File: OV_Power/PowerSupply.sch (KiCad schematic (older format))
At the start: 15 parts, among them J1 OpenVent_Barrel_Connector, U5 CSD88537ND, U6 LTC4365xTS8, U7 LTC4416, U8 AOSD21307, U9 AOSD21307

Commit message: Sorted out the interconnect between power supply and main boards.
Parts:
- added J?: Conn_HDR_2x10_latching, F_Misc:3M_D3428-6302-AR, symbol OpenVent:Conn_HDR_2x10_latching
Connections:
- net labels added: CHG_CURRENT, MOTOR-IN-A, MOTOR-IN-B, PWM, V7.5V, V7.5V_EN, nMOTOR-FAULT-A, nMOTOR-FAULT-B
- wire segments 103 -> 131
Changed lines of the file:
@@
 Text Notes 700  2750 0    50   ~ 0
 INPUT SHOULD BE FUSED.\nA FERRITE MIGHT BE REQUIRED\nFOR EMI SUPPRESSION.\nA TVS SHOULD ALSO BE\nADDED FOR ESD PROTECTION.
+$Comp
+L OpenVent:Conn_HDR_2x10_latching J?
+U 1 1 5FB4D557
+P 2500 5000
+F 0 "J?" H 2550 5617 50  0000 C CNN
+F 1 "Conn_HDR_2x10_latching" H 2550 5526 50  0001 C CNN
+F 2 "F_Misc:3M_D3428-6302-AR" H 2500 5000 50  0001 C CNN
+F 3 "https://multimedia.3m.com/mws/media/485761O/3mtm-four-wall-header-ts2245.pdf" H 2500 5000 50  0001 C CNN
+F 4 "CONN HEADER VERT 20POS 2.54MM LATCHING" H 2500 5000 50  0001 C CNN "Desc"
+F 5 "Connector Header Through Hole 20 position 0.100\" (2.54mm) with latches" H 2500 5000 50  0001 C CNN "Detailed"
+F 6 "3M" H 2500 5000 50  0001 C CNN "Mfr"
+F 7 "D3428-6302-AR" H 2550 5526 50  0000 C CNN "Mfr_PN"
+	1    2500 5000
+	1    0    0    -1
+$EndComp
+$Comp
+L OpenVent:GND #PWR?
+U 1 1 5FB4E8B3
+P 2900 5550
+F 0 "#PWR?" H 2900 5300 50  0001 C CNN
+F 1 "GND" H 2900 5400 50  0001 C CNN
+F 2 "" H 2900 5550 50  0001 C CNN
+F 3 "" H 2900 5550 50  0001 C CNN
+	1    2900 5550
+	1    0    0    -1
+$EndComp
+$Comp
+L OpenVent:GND #PWR?
+U 1 1 5FB4EC42
+P 2000 4500
+F 0 "#PWR?" H 2000 4250 50  0001 C CNN
+F 1 "GND" H 2000 4350 50  0001 C CNN
+F 2 "" H 2000 4500 50  0001 C CNN
+F 3 "" H 2000 4500 50  0001 C CNN
+	1    2000 4500
+	1    0    0    -1
+$EndComp
+$Comp
+L OpenVent:V_MAIN #PWR?
+U 1 1 5FB4F4C3
+P 1850 4500
+F 0 "#PWR?" H 1850 4350 50  0001 C CNN
+F 1 "V_MAIN" H 1850 4673 50  0000 C CNN
+F 2 "" H 1850 4500 50  0001 C CNN
+F 3 "" H 1850 4500 50  0001 C CNN
+	1    1850 4500
+	1    0    0    -1
+$EndComp
+$Comp
+L OpenVent:V_MAIN #PWR?
+U 1 1 5FB4FD2E
+P 3100 4500
+F 0 "#PWR?" H 3100 4350 50  0001 C CNN
+F 1 "V_MAIN" H 3100 4673 50  0000 C CNN
+F 2 "" H 3100 4500 50  0001 C CNN
+F 3 "" H 3100 4500 50  0001 C CNN
+	1    3100 4500
+	1    0    0    -1
+$EndComp
+Text GLabel 1800 5500 0    50   Input ~ 0
+V7.5V
+Text GLabel 3150 5400 2    50   Input ~ 0
+V7.5V
+Text GLabel 3150 5300 2    50   Output ~ 0
+V7.5V_EN
+Wire Wire Line
+	2900 5550 2900 5500
+Wire Wire Line
+	2900 5500 2800 5500
+Wire Wire Line
+	2300 4600 2100 4600
+Wire Wire Line
+	2100 4600 2100 4500
+Wire Wire Line
+	2100 4500 2000 4500
+Wire Wire Line
+	2800 4600 3100 4600
+Wire Wire Line
+	3100 4600 3100 4500
+Wire Wire Line
+	2300 4700 1850 4700
+Wire Wire Line
+	1850 4700 1850 4500
+Wire Wire Line
+	2300 5500 1800 5500
+Wire Wire Line
+	3150 5400 2800 5400
+Wire Wire Line
+	3150 5300 2800 5300
+$Comp
+L OpenVent:VBATT #PWR?
+U 1 1 5FB6E37F
+P 3400 4500
+F 0 "#PWR?" H 3400 4350 50  0001 C CNN
+F 1 "VBATT" H 3400 4673 50  0000 C CNN
+F 2 "" H 3400 4500 50  0001 C CNN
+F 3 "" H 3400 4500 50  0001 C CNN
+	1    3400 4500
+	1    0    0    -1
+$EndComp
+Wire Wire Line
+	2800 4700 3400 4700
+Wire Wire Line
+	3400 4700 3400 4500
+Text GLabel 1800 5000 0    60   Output ~ 0
+PWM
+Text GLabel 1800 4900 0    60   Output ~ 0
+MOTOR-IN-A
+Text GLabel 3150 4900 2    60   Output ~ 0
+MOTOR-IN-B
+Text GLabel 1800 4800 0    60   Input ~ 0
+nMOTOR-FAULT-A
+Text GLabel 3150 4800 2    60   Input ~ 0
+nMOTOR-FAULT-B
+Wire Wire Line
+	4200 2600 4400 2600
+Wire Wire Line
+	1800 4800 2300 4800
+Wire Wire Line
+	2800 4800 3150 4800
+Wire Wire Line
+	1800 4900 2300 4900
+Wire Wire Line
+	3150 4900 2800 4900
+Wire Wire Line
+	2300 5000 1800 5000
+Text GLabel 1800 5400 0    50   Input ~ 0
+CHG_CURRENT
+Wire Wire Line
+	2300 5400 1800 5400
+Wire Wire Line
+	2800 5100 4400 5100
+Wire Wire Line
+	4400 2600 4400 5100
+$Comp
+L OpenVent:GND #PWR?
+U 1 1 5FBAF99A
+P 4300 4950
+F 0 "#PWR?" H 4300 4700 50  0001 C CNN
+F 1 "GND" H 4300 4800 50  0001 C CNN
+F 2 "" H 4300 4950 50  0001 C CNN
+F 3 "" H 4300 4950 50  0001 C CNN
+	1    4300 4950
+	1    0    0    -1
+$EndComp
+Wire Wire Line
+	2800 5000 4150 5000
+Wire Wire Line
+	4150 5000 4150 4950
+Wire Wire Line
+	4150 4950 4300 4950
+$Comp
+L OpenVent:VIN_12V #PWR?
+U 1 1 5FBA1DE1
+P 700 5050
+F 0 "#PWR?" H 700 4900 50  0001 C CNN
+F 1 "VIN_12V" H 700 5223 50  0000 C CNN
+F 2 "" H 700 5050 60  0001 C CNN
+F 3 "" H 700 5050 60  0001 C CNN
+	1    700  5050
+	1    0    0    -1
+$EndComp
+Wire Wire Line
+	2300 5100 700  5100
+Wire Wire Line
+	700  5100 700  5050
 $EndSCHEMATC

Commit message: First cut at a placement study for the power board.
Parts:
- R32, R33, R34, R35, R36, R37, R38, R39: footprint (none) -> Resistor_SMD:R_0603_1608Metric
- gave numbers to parts that had none: 1
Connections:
- net labels added: MOTOR-CURRENT
- wire segments 131 -> 130
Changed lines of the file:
@@
 F 0 "R35" V 3104 2070 50  0000 L CNN
 F 1 "R_0603_510K_0.1W_1%" H 3050 2100 50  0001 C CNN
-F 2 "" H 3050 2100 60  0001 C CNN
+F 2 "Resistor_SMD:R_0603_1608Metric" H 3050 2100 60  0001 C CNN
 F 3 "" H 3050 2100 60  0001 C CNN
 F 4 "510K" V 3195 2070 50  0000 L CNN "Val"
@@
 F 0 "R32" V 2704 2070 50  0000 L CNN
 F 1 "R_0603_4.53M_0.1W_5%" H 2650 2100 50  0001 C CNN
-F 2 "" H 2650 2100 60  0001 C CNN
+F 2 "Resistor_SMD:R_0603_1608Metric" H 2650 2100 60  0001 C CNN
 F 3 "" H 2650 2100 60  0001 C CNN
 F 4 "4.53M" V 2795 2070 50  0000 L CNN "Val"
@@
 F 0 "R33" V 2704 2570 50  0000 L CNN
 F 1 "R_0603_169K_0.1W_1%" H 2650 2600 50  0001 C CNN
-F 2 "" H 2650 2600 60  0001 C CNN
+F 2 "Resistor_SMD:R_0603_1608Metric" H 2650 2600 60  0001 C CNN
 F 3 "" H 2650 2600 60  0001 C CNN
 F 4 "169K" V 2795 2570 50  0000 L CNN "Val"
@@
 F 0 "R34" V 2704 3070 50  0000 L CNN
 F 1 "R_0603_133K_0.1W_1%" H 2650 3100 50  0001 C CNN
-F 2 "" H 2650 3100 60  0001 C CNN
+F 2 "Resistor_SMD:R_0603_1608Metric" H 2650 3100 60  0001 C CNN
 F 3 "" H 2650 3100 60  0001 C CNN
 F 4 "133K" V 2795 3070 50  0000 L CNN "Val"
@@
 F 0 "R39" V 6354 1970 50  0000 L CNN
 F 1 "10k_0603_Chip_Resistor,_1%,_0.1W" H 6300 2000 50  0001 C CNN
-F 2 "" H 6300 2000 50  0001 C CNN
+F 2 "Resistor_SMD:R_0603_1608Metric" H 6300 2000 50  0001 C CNN
 F 3 "" H 6300 2000 50  0001 C CNN
 F 4 "10k" V 6445 1970 50  0000 L CNN "Val"
@@
 F 0 "R37" V 5854 2470 50  0000 L CNN
 F 1 "R_0603_24k9_0.1W_1%" H 5800 2500 50  0001 C CNN
-F 2 "" H 5800 2500 60  0001 C CNN
+F 2 "Resistor_SMD:R_0603_1608Metric" H 5800 2500 60  0001 C CNN
 F 3 "" H 5800 2500 60  0001 C CNN
 F 4 "24k9" V 5945 2470 50  0000 L CNN "Val"
@@
 F 0 "R38" H 5900 3043 50  0000 C CNN
 F 1 "R_0603_221K_0.1W_1%" H 5800 3350 50  0001 C CNN
-F 2 "" H 5800 3350 60  0001 C CNN
+F 2 "Resistor_SMD:R_0603_1608Metric" H 5800 3350 60  0001 C CNN
 F 3 "" H 5800 3350 60  0001 C CNN
 F 4 "221K" H 5900 3134 50  0000 C CNN "Val"
@@
 F 0 "R36" V 5854 1970 50  0000 L CNN
 F 1 "R_0603_178K_0.1W_1%" H 5800 2000 50  0001 C CNN
-F 2 "" H 5800 2000 60  0001 C CNN
+F 2 "Resistor_SMD:R_0603_1608Metric" H 5800 2000 60  0001 C CNN
 F 3 "" H 5800 2000 60  0001 C CNN
 F 4 "178K" V 5945 1970 50  0000 L CNN "Val"
@@
 INPUT SHOULD BE FUSED.\nA FERRITE MIGHT BE REQUIRED\nFOR EMI SUPPRESSION.\nA TVS SHOULD ALSO BE\nADDED FOR ESD PROTECTION.
 $Comp
-L OpenVent:Conn_HDR_2x10_latching J?
+L OpenVent:Conn_HDR_2x10_latching J2
 U 1 1 5FB4D557
 P 2500 5000
-F 0 "J?" H 2550 5617 50  0000 C CNN
+F 0 "J2" H 2550 5617 50  0000 C CNN
 F 1 "Conn_HDR_2x10_latching" H 2550 5526 50  0001 C CNN
 F 2 "F_Misc:3M_D3428-6302-AR" H 2500 5000 50  0001 C CNN
@@
 $EndComp
 $Comp
-L OpenVent:GND #PWR?
+L OpenVent:GND #PWR030
 U 1 1 5FB4E8B3
 P 2900 5550
-F 0 "#PWR?" H 2900 5300 50  0001 C CNN
+F 0 "#PWR030" H 2900 5300 50  0001 C CNN
 F 1 "GND" H 2900 5400 50  0001 C CNN
 F 2 "" H 2900 5550 50  0001 C CNN
@@
 $EndComp
 $Comp
-L OpenVent:GND #PWR?
+L OpenVent:GND #PWR018
 U 1 1 5FB4EC42
 P 2000 4500
-F 0 "#PWR?" H 2000 4250 50  0001 C CNN
+F 0 "#PWR018" H 2000 4250 50  0001 C CNN
 F 1 "GND" H 2000 4350 50  0001 C CNN
 F 2 "" H 2000 4500 50  0001 C CNN
@@
 $EndComp
 $Comp
-L OpenVent:V_MAIN #PWR?
-U 1 1 5FB4F4C3
-P 1850 4500
-F 0 "#PWR?" H 1850 4350 50  0001 C CNN
-F 1 "V_MAIN" H 1850 4673 50  0000 C CNN
-F 2 "" H 1850 4500 50  0001 C CNN
-F 3 "" H 1850 4500 50  0001 C CNN
-	1    1850 4500
-	1    0    0    -1
-$EndComp
-$Comp
-L OpenVent:V_MAIN #PWR?
+L OpenVent:V_MAIN #PWR031
 U 1 1 5FB4FD2E
 P 3100 4500
-F 0 "#PWR?" H 3100 4350 50  0001 C CNN
+F 0 "#PWR031" H 3100 4350 50  0001 C CNN
 F 1 "V_MAIN" H 3100 4673 50  0000 C CNN
 F 2 "" H 3100 4500 50  0001 C CNN
@@
 	3100 4600 3100 4500
 Wire Wire Line
-	2300 4700 1850 4700
-Wire Wire Line
-	1850 4700 1850 4500
-Wire Wire Line
 	2300 5500 1800 5500
 Wire Wire Line
@@
 	3150 5300 2800 5300
 $Comp
-L OpenVent:VBATT #PWR?
+L OpenVent:VBATT #PWR032
 U 1 1 5FB6E37F
 P 3400 4500
-F 0 "#PWR?" H 3400 4350 50  0001 C CNN
+F 0 "#PWR032" H 3400 4350 50  0001 C CNN
 F 1 "VBATT" H 3400 4673 50  0000 C CNN
 F 2 "" H 3400 4500 50  0001 C CNN
@@
 	4400 2600 4400 5100
 $Comp
-L OpenVent:GND #PWR?
+L OpenVent:GND #PWR033
 U 1 1 5FBAF99A
 P 4300 4950
-F 0 "#PWR?" H 4300 4700 50  0001 C CNN
+F 0 "#PWR033" H 4300 4700 50  0001 C CNN
 F 1 "GND" H 4300 4800 50  0001 C CNN
 F 2 "" H 4300 4950 50  0001 C CNN
@@
 	4150 4950 4300 4950
 $Comp
-L OpenVent:VIN_12V #PWR?
+L OpenVent:VIN_12V #PWR017
 U 1 1 5FBA1DE1
 P 700 5050
-F 0 "#PWR?" H 700 4900 50  0001 C CNN
+F 0 "#PWR017" H 700 4900 50  0001 C CNN
 F 1 "VIN_12V" H 700 5223 50  0000 C CNN
 F 2 "" H 700 5050 60  0001 C CNN
@@
 Wire Wire Line
 	700  5100 700  5050
+Text GLabel 1800 5200 0    50   Input ~ 0
+MOTOR-CURRENT
+Wire Wire Line
+	2300 5200 1800 5200
 $EndSCHEMATC

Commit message: New board outline and power connector added.  Still need definition of connector for microswitches and schematic.
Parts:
- removed J1: OpenVent_Barrel_Connector, Connector_BarrelJack:BarrelJack_CUI_PJ-102AH_Horizontal, symbol OpenVent:OpenVent_Barrel_Connector
- added J1: Kycon_kpjx-4s, OpenVent:Kycon_KPJX-4S, symbol OpenVent:Kycon_kpjx-4s
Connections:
- wire segments 130 -> 140
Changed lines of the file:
@@
 L OpenVent:GND #GND_?
 U 1 1 5FBB7C1D
-P 1400 2200
+P 1050 2050
 AR Path="/5FBB7C1D" Ref="#GND_?"  Part="1"
 AR Path="/5FAE643E/5FBB7C1D" Ref="#GND_017"  Part="1"
-F 0 "#GND_017" H 1400 2200 20  0001 C CNN
-F 1 "GND" H 1400 2130 30  0001 C CNN
-F 2 "" H 1400 2200 70  0001 C CNN
-F 3 "" H 1400 2200 70  0001 C CNN
-	1    1400 2200
-	1    0    0    -1
-$EndComp
-Wire Wire Line
-	1400 1900 1150 1900
-$Comp
-L OpenVent:OpenVent_Barrel_Connector J?
-U 1 1 5FBB7C29
-P 1050 1900
-AR Path="/5FBB7C29" Ref="J?"  Part="1"
-AR Path="/5FAE643E/5FBB7C29" Ref="J1"  Part="1"
-F 0 "J1" H 957 2325 50  0000 C CNN
-F 1 "OpenVent_Barrel_Connector" H 740 1770 50  0001 L BNN
-F 2 "Connector_BarrelJack:BarrelJack_CUI_PJ-102AH_Horizontal" H 1050 1900 50  0001 C CNN
-F 3 "https://www.cuidevices.com/product/resource/digikeypdf/pj-102ah.pdf" H 1050 1900 50  0001 C CNN
-F 4 "PJ-102AH" H 957 2234 50  0000 C CNN "Mfr_PN"
-F 5 "CUI Devices" H 1050 1900 50  0001 C CNN "Mfr"
-F 6 "DigiKey" H 1050 1900 50  0001 C CNN "DistName"
-F 7 "CP-102AH-ND" H 1050 1900 50  0001 C CNN "Dist_PN"
-F 8 "Power Barrel Connector Jack 2.00mm ID (0.079\"), 5.50mm OD (0.217\") Through Hole, Right Angle" H 1050 1900 50  0001 C CNN "Detailed"
-	1    1050 1900
-	1    0    0    -1
-$EndComp
-Wire Wire Line
-	1400 1900 1400 2200
-Wire Wire Line
-	1150 1700 2550 1700
-Connection ~ 2550 1700
-Text Notes 1200 1250 0    50   ~ 0
+F 0 "#GND_017" H 1050 2050 20  0001 C CNN
+F 1 "GND" H 1050 1980 30  0001 C CNN
+F 2 "" H 1050 2050 70  0001 C CNN
+F 3 "" H 1050 2050 70  0001 C CNN
+	1    1050 2050
+	1    0    0    -1
+$EndComp
+Text Notes 1050 950  0    50   ~ 0
 LTC4365 provides reverse polarity protection\nUndervoltage lockout: 8V\nOvervoltage lockout: 18V
 Wire Notes Line
-	1150 950  3000 950
+	1000 650  2850 650
 Wire Notes Line
-	3000 950  3000 1300
+	2850 650  2850 1000
 Wire Notes Line
-	3000 1300 1150 1300
+	2850 1000 1000 1000
 Wire Notes Line
-	1150 1300 1150 950
+	1000 1000 1000 650
 $Comp
 L OpenVent:LTC4416 U7
@@
 	6750 3700 6750 3650
 Connection ~ 7150 3400
-Text Notes 700  2750 0    50   ~ 0
+Text Notes 600  2650 0    50   ~ 0
 INPUT SHOULD BE FUSED.\nA FERRITE MIGHT BE REQUIRED\nFOR EMI SUPPRESSION.\nA TVS SHOULD ALSO BE\nADDED FOR ESD PROTECTION.
 $Comp
@@
 Wire Wire Line
 	2300 5200 1800 5200
+$Comp
+L OpenVent:Kycon_kpjx-4s J1
+U 1 1 5FBCEB95
+P 1050 1700
+F 0 "J1" H 1050 2067 50  0000 C CNN
+F 1 "Kycon_kpjx-4s" H 1050 1976 50  0000 C CNN
+F 2 "OpenVent:Kycon_KPJX-4S" H 1050 1700 50  0001 C CNN
+F 3 "http://www.kycon.com/Pub_Eng_Draw/KPJX-4S.pdf" H 1050 1700 50  0001 C CNN
+F 4 "Kycon, Inc." H 1050 1700 50  0001 C CNN "Mfr"
+F 5 "KPJX-4S" H 1050 1700 50  0001 C CNN "Mfr_PN"
+F 6 "4 (Power) Position Circular Connector Jack, Female Sockets Solder" H 1050 1700 50  0001 C CNN "Detailed"
+F 7 "CONN JACK FMALE 4POS TIN SOLDER" H 1050 1700 50  0001 C CNN "Desc"
+	1    1050 1700
+	1    0    0    -1
+$EndComp
+Wire Wire Line
+	2550 1700 1500 1700
+Connection ~ 2550 1700
+Wire Wire Line
+	750  1600 650  1600
+Wire Wire Line
+	650  1600 650  1250
+Wire Wire Line
+	650  1250 1500 1250
+Wire Wire Line
+	1500 1250 1500 1700
+Connection ~ 1500 1700
+Wire Wire Line
+	1500 1700 1350 1700
+Wire Wire Line
+	1350 1600 1400 1600
+Wire Wire Line
+	1400 1600 1400 2000
+Wire Wire Line
+	1400 2000 1050 2000
+Wire Wire Line
+	700  2000 700  1700
+Wire Wire Line
+	700  1700 750  1700
+Wire Wire Line
+	1050 2000 1050 2050
+Connection ~ 1050 2000
+Wire Wire Line
+	1050 2000 700  2000
 $EndSCHEMATC

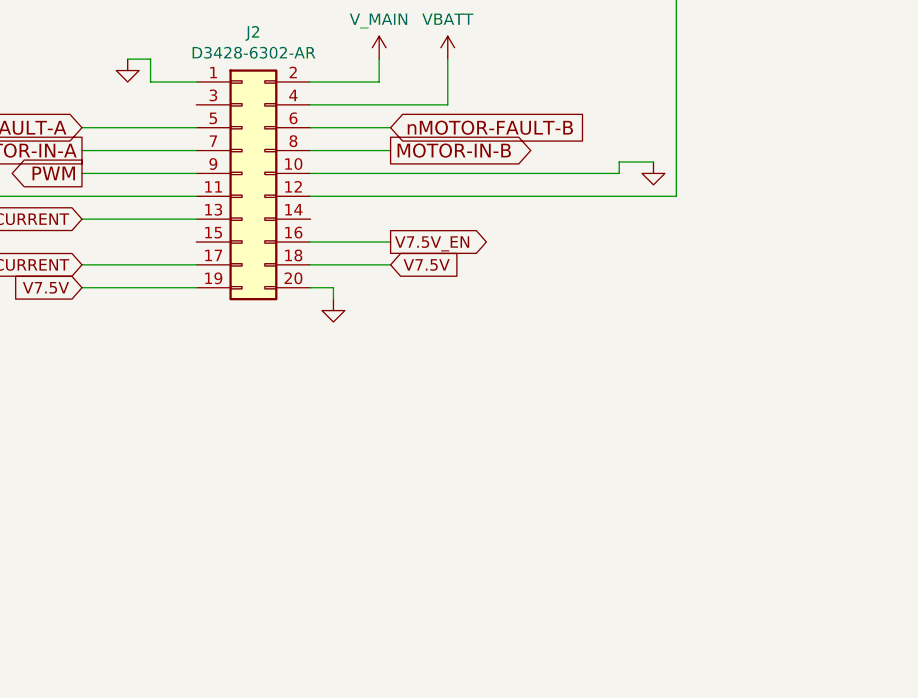
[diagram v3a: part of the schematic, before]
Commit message: Continuing to refine both the schemo and placement for the power supply board.  I think we have all the connectors we need now...
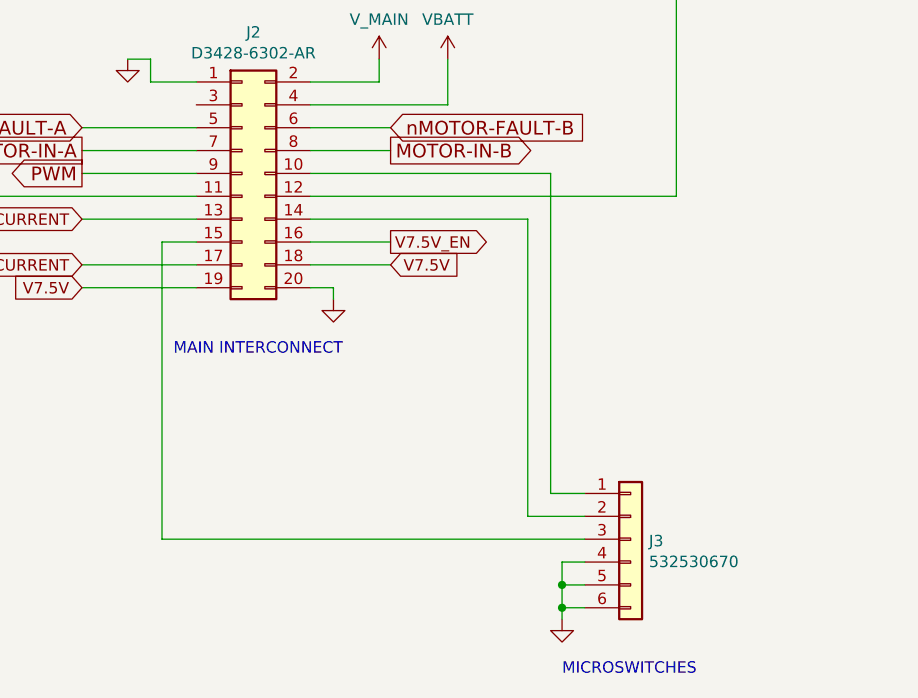
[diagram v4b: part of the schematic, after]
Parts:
- added J3: 532530670, Connector_Molex:Molex_Micro-Latch_53253-0670_1x06_P2.00mm_Vertical, symbol OpenVent:532530670
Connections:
- wire segments 140 -> 152
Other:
- note added: "MAIN INTERCONNECT"
- note added: "MICROSWITCHES"
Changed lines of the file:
@@
 	4400 2600 4400 5100
-$Comp
-L OpenVent:GND #PWR033
-U 1 1 5FBAF99A
-P 4300 4950
-F 0 "#PWR033" H 4300 4700 50  0001 C CNN
-F 1 "GND" H 4300 4800 50  0001 C CNN
-F 2 "" H 4300 4950 50  0001 C CNN
-F 3 "" H 4300 4950 50  0001 C CNN
-	1    4300 4950
-	1    0    0    -1
-$EndComp
-Wire Wire Line
-	2800 5000 4150 5000
-Wire Wire Line
-	4150 5000 4150 4950
-Wire Wire Line
-	4150 4950 4300 4950
 $Comp
 L OpenVent:VIN_12V #PWR017
@@
 Wire Wire Line
 	1050 2000 700  2000
+$Comp
+L OpenVent:532530670 J3
+U 1 1 5FC7E477
+P 4200 6600
+F 0 "J3" H 4280 6592 50  0000 L CNN
+F 1 "532530670" H 4280 6501 50  0000 L CNN
+F 2 "Connector_Molex:Molex_Micro-Latch_53253-0670_1x06_P2.00mm_Vertical" H 4200 6600 50  0001 C CNN
+F 3 "https://www.molex.com/pdm_docs/sd/532530270_sd.pdf" H 4200 6600 50  0001 C CNN
+F 4 "Molex" H 4200 6600 50  0001 C CNN "Mfr"
+F 5 "0532530670" H 4200 6600 50  0001 C CNN "Mfr_PN"
+F 6 "CONN HEADER VERT 6POS 2MM" H 4200 6600 50  0001 C CNN "Desc"
+F 7 "Connector Header Through Hole 6 position 0.079\" (2.00mm)" H 4200 6600 50  0001 C CNN "Detailed"
+	1    4200 6600
+	1    0    0    -1
+$EndComp
+$Comp
+L OpenVent:GND #PWR033
+U 1 1 5FC7F729
+P 3900 6950
+F 0 "#PWR033" H 3900 6700 50  0001 C CNN
+F 1 "GND" H 3900 6800 50  0001 C CNN
+F 2 "" H 3900 6950 50  0001 C CNN
+F 3 "" H 3900 6950 50  0001 C CNN
+	1    3900 6950
+	1    0    0    -1
+$EndComp
+Wire Wire Line
+	4000 6700 3900 6700
+Wire Wire Line
+	3900 6700 3900 6800
+Wire Wire Line
+	4000 6800 3900 6800
+Connection ~ 3900 6800
+Wire Wire Line
+	3900 6800 3900 6900
+Wire Wire Line
+	4000 6900 3900 6900
+Connection ~ 3900 6900
+Wire Wire Line
+	3900 6900 3900 6950
+Wire Wire Line
+	4000 6600 2150 6600
+Wire Wire Line
+	2150 6600 2150 5300
+Wire Wire Line
+	2150 5300 2300 5300
+Wire Wire Line
+	4000 6500 3750 6500
+Wire Wire Line
+	3750 6500 3750 5200
+Wire Wire Line
+	3750 5200 2800 5200
+Wire Wire Line
+	2800 5000 3850 5000
+Wire Wire Line
+	3850 5000 3850 6400
+Wire Wire Line
+	3850 6400 4000 6400
+Text Notes 2200 5800 0    50   ~ 0
+MAIN INTERCONNECT
+Text Notes 3900 7200 0    50   ~ 0
+MICROSWITCHES
 $EndSCHEMATC

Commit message: Added two connectors for cooling fans, re-jigged the motor current sensing circuit a bit, still needs a bit of work there.
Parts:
- removed R32: R_0603_4.53M_0.1W_5%, Resistor_SMD:R_0603_1608Metric, symbol OpenVent:R_0603_4.53M_0.1W_5%
- removed R33: R_0603_169K_0.1W_1%, Resistor_SMD:R_0603_1608Metric, symbol OpenVent:R_0603_169K_0.1W_1%
- removed R34: R_0603_133K_0.1W_1%, Resistor_SMD:R_0603_1608Metric, symbol OpenVent:R_0603_133K_0.1W_1%
- removed R35: R_0603_510K_0.1W_1%, Resistor_SMD:R_0603_1608Metric, symbol OpenVent:R_0603_510K_0.1W_1%
- removed U5: CSD88537ND, Package_SO:SOIC-8_3.9x4.9mm_P1.27mm, symbol OpenVent:CSD88537ND
- removed U6: LTC4365xTS8, Package_TO_SOT_SMD:TSOT-23-8, symbol Power_Management:LTC4365xTS8
- added J6, J7: CONN_HEADER_2.54X2_MOLEX_KK_Series, Connector_Molex:Molex_KK-254_AE-6410-02A_1x02_P2.54mm_Vertical, symbol OpenVent:CONN_HEADER_2.54X2_MOLEX_KK_Series
- added Q3, Q4: SZNUD3124LT1G, Package_TO_SOT_SMD:SOT-23, symbol OpenVent:SZNUD3124LT1G
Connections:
- net labels added: FAN_DRIVE
- wire segments 152 -> 127
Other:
- note added: "FAN CONNECTIONS"
- note added: "Static drain on VBATT when input power disconnected\nis approximately 16 to 17uA with U9 active\nand connected to V_MAIN."
- moved on the sheet: C13, R36, R37, R38, R39, U7, U8A, U8B, U9A, U9B
